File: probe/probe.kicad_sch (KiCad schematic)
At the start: 7 parts, among them J1 To circuit, J2 To scope

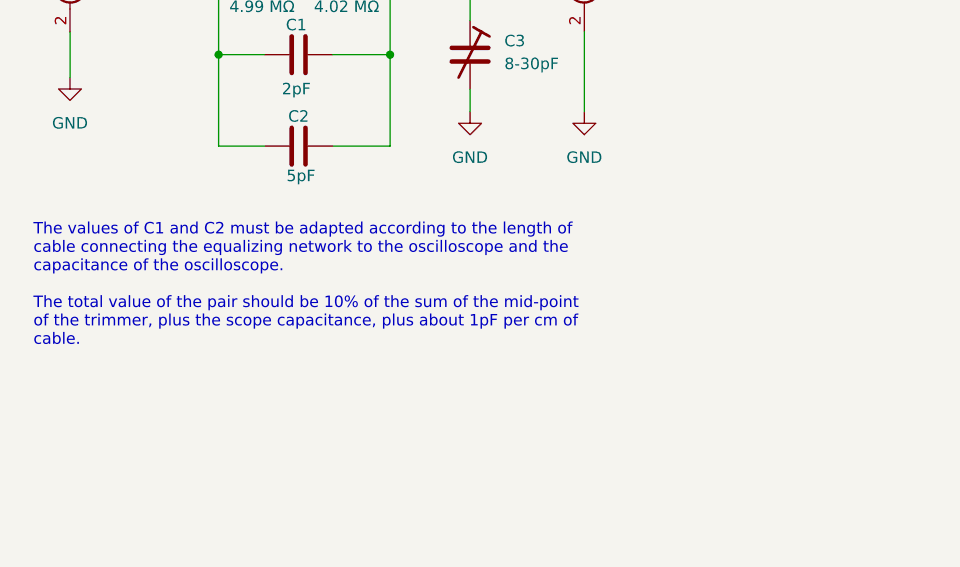
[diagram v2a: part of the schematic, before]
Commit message: Added clarifying note to schematic.
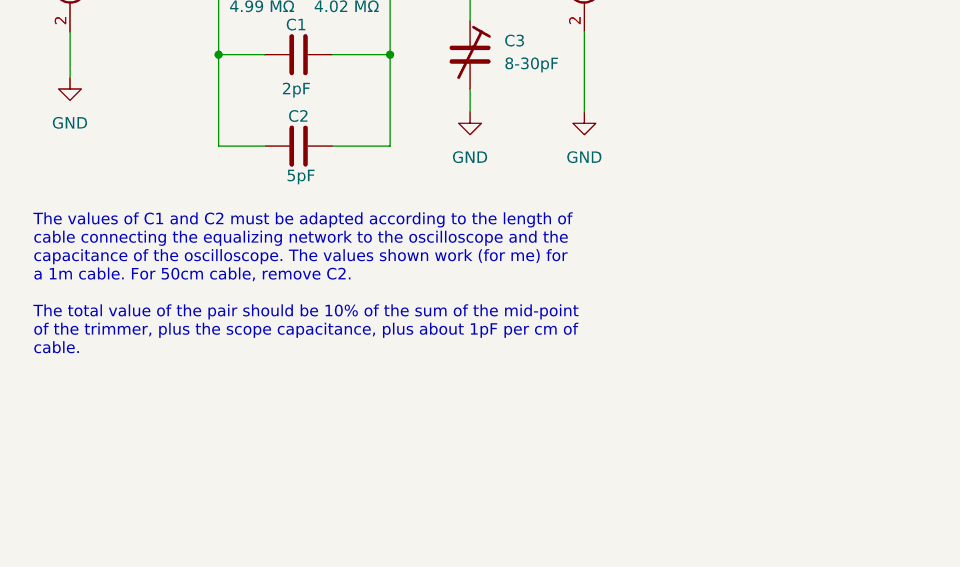
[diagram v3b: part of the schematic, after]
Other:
- note added: "The values of C1 and C2 must be adapted according to the length of cable connecting the equalizing network to the oscilloscope and the capacitance of the oscilloscope. The values shown work (for me) for a 1m cable. For 50cm cable, remove C2. The total value of the pair should be 10% of the sum of the mid-point of the trimmer, plus the scope capacitance, plus about 1pF per cm of cable."
- note removed: "The values of C1 and C2 must be adapted according to the length of cable connecting the equalizing network to the oscilloscope and the capacitance of the oscilloscope. The total value of the pair should be 10% of the sum of the mid-point of the trimmer, plus the scope capacitance, plus about 1pF per cm of cable."
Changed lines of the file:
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@@
 	(generator_version "9.0")
 	(paper "A4")
-	(text "The values of C1 and C2 must be adapted according to the length of \ncable connecting the equalizing network to the oscilloscope and the\ncapacitance of the oscilloscope.\n\nThe total value of the pair should be 10% of the sum of the mid-point\nof the trimmer, plus the scope capacitance, plus about 1pF per cm of\ncable."
+	(text "The values of C1 and C2 must be adapted according to the length of \ncable connecting the equalizing network to the oscilloscope and the\ncapacitance of the oscilloscope. The values shown work (for me) for\na 1m cable. For 50cm cable, remove C2.\n\nThe total value of the pair should be 10% of the sum of the mid-point\nof the trimmer, plus the scope capacitance, plus about 1pF per cm of\ncable."
 		(exclude_from_sim no)
 		(at 98.806 113.284 0)
